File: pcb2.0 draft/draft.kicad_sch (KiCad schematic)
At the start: 24 parts, among them J1 Screw_Terminal_01x02, J2 Screw_Terminal_01x02, J3 Conn_01x04, J4 Conn_01x04, J5 Conn_01x04, U1 ESP32-DevKitC, U2 LM2576HVS-5, U3 LM2576HVS-3.3

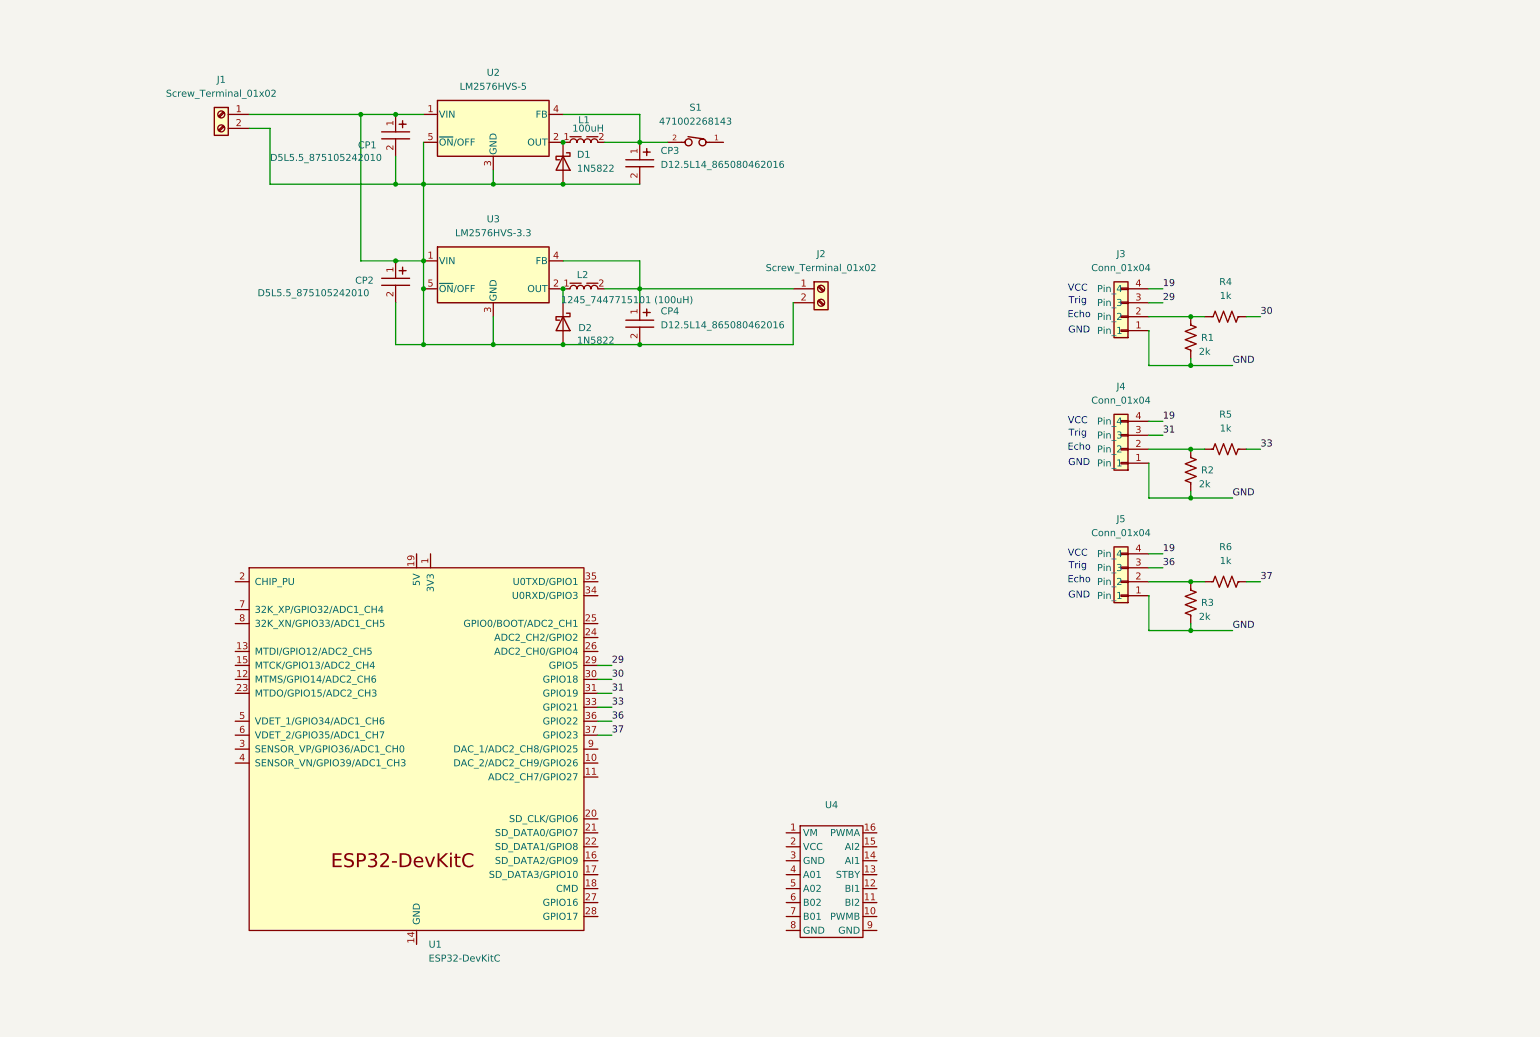
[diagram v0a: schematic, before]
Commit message: completed draft of pcbv2 - in "draft" folder
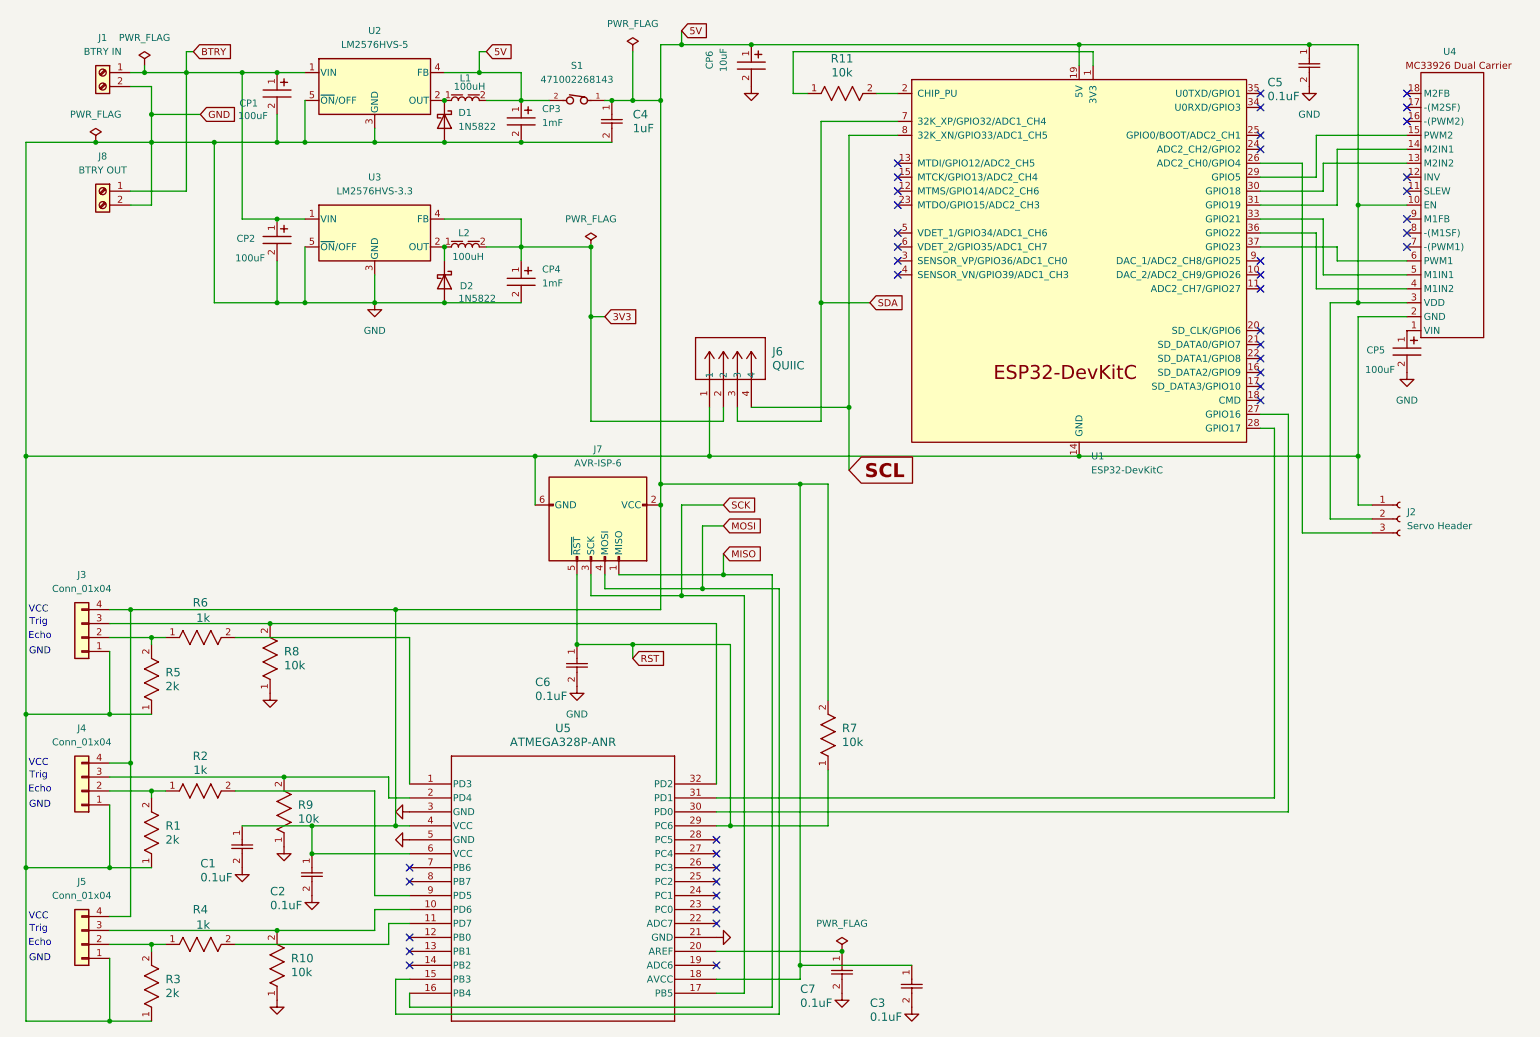
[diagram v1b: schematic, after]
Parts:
- removed J2: Screw_Terminal_01x02, terminal:CUI_TB002-500-02BE, symbol Connector:Screw_Terminal_01x02
- removed R1, R2, R3: 2k, Resistor_THT:R_Axial_DIN0207_L6.3mm_D2.5mm_P5.08mm_Vertical, symbol Device:R_US
- removed R4: 1k, Resistor_THT:R_Axial_DIN0207_L6.3mm_D2.5mm_P2.54mm_Vertical, symbol Device:R_US
- removed R5, R6: 1k, Resistor_THT:R_Axial_DIN0207_L6.3mm_D2.5mm_P5.08mm_Vertical, symbol Device:R_US
- removed U4: ~, custom:TB6612FNG_BoB, symbol custom:TB6612FNG_BoB
- added C1, C2, C3, C5, C6, C7: 0.1uF, G-188_MUR, symbol cap_murata_0603:GCM188R71C104KA37D
- added C4: 1uF, CAP_GRM21_MUR, symbol cap_murata_0805:GRM21BR71C105KA01L
- added CP5: 100uF, Capacitor_SMD_Wurth:CP_Wurth_WCAP-PSLP-D5L5.5, symbol WurthE:D5L5.5_875105242010
- added CP6: 10uF, Capacitor_SMD_Wurth:CP_Wurth_WCAP-PSLP-D5L5.8, symbol WurthE:D5L5.8_875105359001
- added J2: Servo Header, Connector_PinSocket_2.54mm:PinSocket_1x03_P2.54mm_Vertical, symbol Connector:Conn_01x03_Socket
- added J6: QUIIC, CONN_SM04B-SRSS-TB_JST, symbol quiic_jst:SM04B-SRSS-TB
- added J7: AVR-ISP-6, Connector_IDC:IDC-Header_2x03_P2.54mm_Vertical, symbol Connector:AVR-ISP-6
- added J8: BTRY OUT, terminal:CUI_TB002-500-02BE, symbol Connector:Screw_Terminal_01x02
- added R1, R3, R5: 2k, RES_CR0805_VEN, symbol R_SMD:CR0805-10W-2001FT
- added R10, R11, R7, R8, R9: 10k, RES_CR0805_VEN, symbol R_SMD:CR0805-10W-2001FT
- added R2, R4, R6: 1k, RES_CR0805_VEN, symbol R_SMD:CR0805-10W-2001FT
- added U4: ~, polulu_MC33926_dual:polulu_MC33926_dual, symbol polulu_MC33926_dual:MC33926_dual
- added U5: ATMEGA328P-ANR, 32A_ATM, symbol atmega328p-anr:ATMEGA328P-ANR
- CP1, CP2: value D5L5.5_875105242010 -> 100uF; footprint WurthE:CP_Wurth_WCAP-PSLP-D5L5.5 -> Capacitor_SMD_Wurth:CP_Wurth_WCAP-PSLP-D5L5.5
- CP3, CP4: value D12.5L14_865080462016 -> 1mF; footprint WurthE:CP_Wurth_WCAP-ASLI-D12.5L14 -> Capacitor_SMD_Wurth:CP_Wurth_WCAP-ASLI-D12.5L14
- J1: value Screw_Terminal_01x02 -> BTRY IN
- L1: footprint WE-PD:L_Wurth_WE-PD-1245 -> Inductor_SMD_Wurth:L_Wurth_WE-PD-1245
- L2: value 1245_7447715101 (100uH) -> 100uH; footprint WE-PD:L_Wurth_WE-PD-1245 -> Inductor_SMD_Wurth:L_Wurth_WE-PD-1245
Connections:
- net 19 is gone; now on net 5V: J3.4 (Pin_4), J4.4 (Pin_4), J5.4 (Pin_4)
- net GND: now also CP1.2, CP2.2, CP3.2, CP4.2, D1.2 (A), D2.2 (A), J1.2 (Pin_2), U1.14 (GND), U1.32 (GND), U1.38 (GND), U2.3 (GND), U2.5 (~{ON}/OFF), U3.3 (GND), U3.5 (~{ON}/OFF), C1.2, C2.2, C3.2, C4.2, C5.2, C6.2, C7.2, CP5.2, CP6.2, J2.1 (Pin_1), J6.1, J7.6 (GND), J8.2 (Pin_2), R1.1, R10.1, R3.1, R5.1, R8.1, R9.1, U4.2 (GND), U5.21 (GND), U5.3 (GND), U5.5 (GND)
- net at J5.2 (Pin_2): now also R3.2, R4.1
- net 5V: now reaches CP3.1, L1.2, S1.2, U2.4 (FB)
- net 5V: now also S1.1, U1.19 (5V), C1.1, C2.1, C3.1, C4.1, C5.1, CP6.1, J2.2 (Pin_2), J7.2 (VCC), R7.2, U4.10 (EN), U4.3 (VDD), U5.18 (AVCC), U5.4 (VCC), U5.6 (VCC)
- net 3V3: now reaches CP4.1, L2.2, U3.4 (FB)
- net 3V3: now also J6.2
- net at J3.2 (Pin_2): now also R5.2, R6.1
- net at J4.2 (Pin_2): now also R1.2, R2.1
- net at U1.1 (3V3): now also R11.1
- net at U1.2 (CHIP_PU): now also R11.2
- net at U1.26 (ADC2_CH0/GPIO4): now also J2.3 (Pin_3)
- net at U1.27 (GPIO16): now also U5.30 (PD0)
- net at U1.28 (GPIO17): now also U5.31 (PD1)
- net SDA: now reaches U1.7 (32K_XP/GPIO32/ADC1_CH4)
- net SDA: now also J6.3
- net SCL: now reaches U1.8 (32K_XN/GPIO33/ADC1_CH5)
- net SCL: now also J6.4
- net 29: no longer names the net of J3.3 (Pin_3)
- net 29: now also R8.2, U5.32 (PD2); no longer U1.29 (GPIO5)
- net 30: no longer names the net of U1.30 (GPIO18)
- net 30: now also U4.13 (M2IN2)
- net 31: no longer names the net of J4.3 (Pin_3)
- net 31: now also R9.2, U5.2 (PD4); no longer U1.31 (GPIO19)
- net 33: no longer names the net of U1.33 (GPIO21)
- net 33: now also U4.5 (M1IN1)
- net 36: no longer names the net of J5.3 (Pin_3)
- net 36: now also R10.2, U5.10 (PD6); no longer U1.36 (GPIO22)
- net 37: no longer names the net of U1.37 (GPIO23)
- net 37: now also U4.6 (PWM1)
- new net: R6.2, U5.1 (PD3)
- new net: R4.2, U5.11 (PD7)
- new net: C7.1, U5.20 (AREF)
- new net: R2.2, U5.9 (PD5)
- new net: U1.29 (GPIO5), U4.15 (PWM2)
- new net: U1.31 (GPIO19), U4.14 (M2IN1)
- new net: U1.36 (GPIO22), U4.4 (M1IN2)
- new net: CP5.1, U4.1 (VIN)
- new net BTRY: CP1.1, CP2.1, J1.1 (Pin_1), J8.1 (Pin_1), U2.1 (VIN), U3.1 (VIN)
- new net MISO: J7.1 (MISO), U5.16 (PB4)
- new net MOSI: J7.4 (MOSI), U5.15 (PB3)
- new net RST: C6.1, J7.5 (~{RST}), R7.1, U5.29 (PC6)
- new net SCK: J7.3 (SCK), U5.17 (PB5)
- no-connect marks 0 -> 42
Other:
- title: (none) -> PCB Version 2.0
- moved on the sheet: CP1, CP2, CP3, CP4, D1, D2, J1, L1, L2, S1, U1, U2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

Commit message: some more schematic updates
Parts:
- removed S1: 471002268143, WE-RSTV:switch_471002268143_actual, symbol WE-RSTV:471002268143
- added C8: 1uF, CAP_GRM21_MUR, symbol cap_murata_0805:GRM21BR71C105KA01L
- added LED1, LED2, LED3, LED4: EAST3215BA3, LEDC3215X110N, symbol Everlight_LED_1206:EAST3215BA3
- added R12: 1.2k, ERJU08J122V:RES_ERJU08J122V, symbol R_panasonic_1206_1p2k:ERJU08J122V
- added R13: 620, RC1206N_PAN, symbol R_panasonic_1206_620:ERJ-P08J621V
- added R14, R15: 270, ERJU08J271V:RES_ERJU08J271V, symbol R_panasonic_1206_270:ERJU08J271V
- added R16, R17: 10k, RES_CR0805_VEN, symbol R_SMD:CR0805-10W-2001FT
- added S2, S3: EG2201B, EG2201B:SW_EG2201B, symbol SW_eswitch_dpdt_eg2201:EG2201B
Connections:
- net 3V3: now also C1.1, C2.1, C3.1, J3.4 (Pin_4), J4.4 (Pin_4), J5.4 (Pin_4), J7.2 (VCC), R7.2, U5.18 (AVCC), U5.4 (VCC), U5.6 (VCC), C8.1, LED3.2 (A), S3.4, S3.5
- net 5V: now also LED2.2 (A), S3.1, S3.2; no longer C1.1, C2.1, C3.1, J3.4 (Pin_4), J4.4 (Pin_4), J5.4 (Pin_4), J7.2 (VCC), R7.2, U5.18 (AVCC), U5.4 (VCC), U5.6 (VCC)
- net BTRY: now also LED1.2 (A)
- net GND: now also C8.2, R12.1, R13.2, R14.2, R15.2, R16.1, R17.1
- net at U5.27 (PC4): now also LED4.2 (A)
- net at U5.30 (PD0): now also S2.5; no longer U1.27 (GPIO16)
- net at U5.31 (PD1): now also S2.2; no longer U1.28 (GPIO17)
- new net: R17.2, S2.6
- new net: LED4.1 (K), R15.1
- new net: S2.1, U1.28 (GPIO17)
- new net: R16.2, S2.3
- new net: S2.4, U1.27 (GPIO16)
- new net: LED1.1 (K), R12.2
- new net: LED2.1 (K), R13.1
- new net: LED3.1 (K), R14.1
- no-connect marks 42 -> 41
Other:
- note added: "ADD REVERSE POLARITY PROTECTION"
- moved on the sheet: C4, CP6

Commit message: completed pcb layout
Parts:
- removed J1: BTRY IN, terminal:CUI_TB002-500-02BE, symbol Connector:Screw_Terminal_01x02
- removed J8: BTRY OUT, terminal:CUI_TB002-500-02BE, symbol Connector:Screw_Terminal_01x02
- added J1: BTRY IN, jst_xh:JST_B2B-XH-A, symbol JST_XH-A:B2B-XH-A
- added J8: BTRY OUT, jst_xh:JST_B2B-XH-A, symbol JST_XH-A:B2B-XH-A
- C1, C2, C3, C5, C6, C7: footprint G-188_MUR -> cap_murata_0603:G-188_MUR-L
- C4, C8: footprint CAP_GRM21_MUR -> cap_murata_0805:CAP_GRM21_MUR-L
- CP1, CP2, CP5: footprint Capacitor_SMD_Wurth:CP_Wurth_WCAP-PSLP-D5L5.5 -> WurthE:CP_Wurth_WCAP-PSLP-D5L5.5
- CP3, CP4: footprint Capacitor_SMD_Wurth:CP_Wurth_WCAP-ASLI-D12.5L14 -> WurthE:CP_Wurth_WCAP-ASLI-D12.5L14
- CP6: footprint Capacitor_SMD_Wurth:CP_Wurth_WCAP-PSLP-D5L5.8 -> WurthE:CP_Wurth_WCAP-PSLP-D5L5.8
- J6: footprint CONN_SM04B-SRSS-TB_JST -> quiic_jst:CONN_SM04B-SRSS-TB_JST
- L1, L2: footprint Inductor_SMD_Wurth:L_Wurth_WE-PD-1245 -> WE-PD:L_Wurth_WE-PD-1245
- LED1, LED2, LED3, LED4: footprint LEDC3215X110N -> led_smd_1206:LEDC3215X110N
- R1, R10, R11, R16, R17, R2, R3, R4, R5, R6, R7, R8, R9: footprint RES_CR0805_VEN -> R_SMD:RES_CR0805_VEN-L
- R12: footprint ERJU08J122V:RES_ERJU08J122V -> r_erj_1p2k:RES_ERJU08J122V
- R13: footprint RC1206N_PAN -> R_ERJ_620_1206:RC1206N_PAN-L
- R14, R15: footprint ERJU08J271V:RES_ERJU08J271V -> r_erj_270:RES_ERJU08J271V
- S2, S3: footprint EG2201B:SW_EG2201B -> switch_eg2201_dpdt:SW_EG2201B
- U5: footprint 32A_ATM -> atmega328p-anr:32A_ATM-L
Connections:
- net 3V3: no longer CP4.1, L2.2, S3.5, U3.4 (FB)
- net 5V: no longer CP3.1, L1.2, S3.2, U2.4 (FB)
- net BTRY: now also J1.2, J8.2
- net GND: now also J1.1, J8.1
- new net 3V30: CP4.1, L2.2, S3.5, U3.4 (FB)
- new net 5V0: CP3.1, L1.2, S3.2, U2.4 (FB)
- no-connect marks 41 -> 43

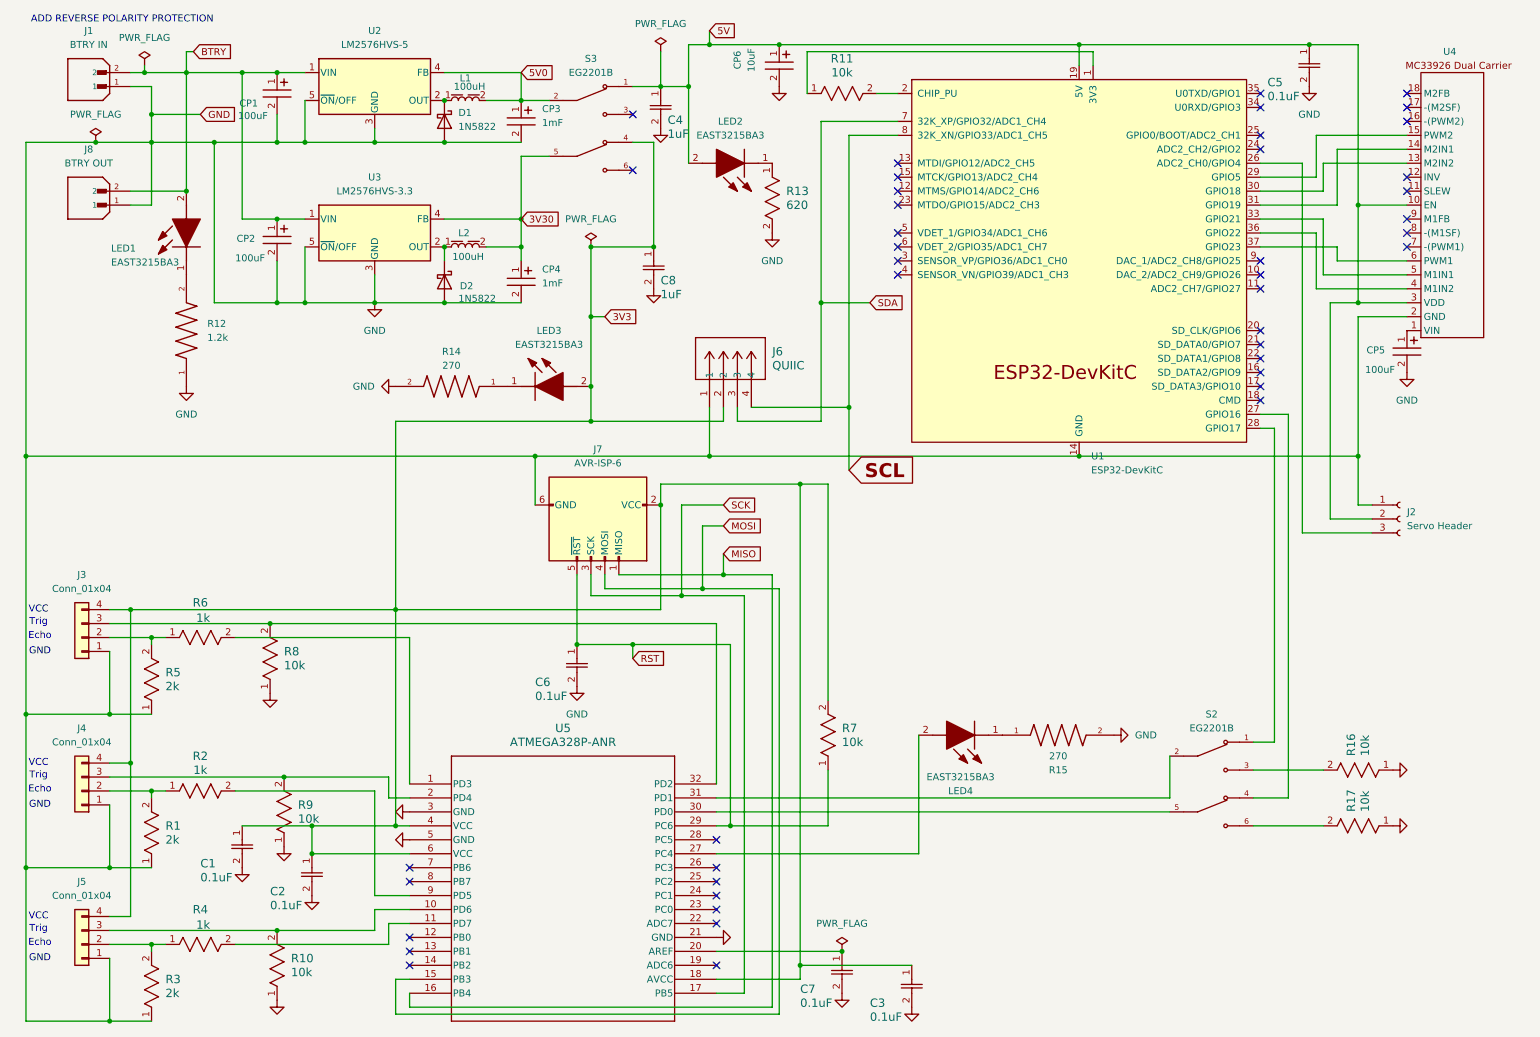
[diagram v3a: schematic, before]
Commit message: broke out code into header files
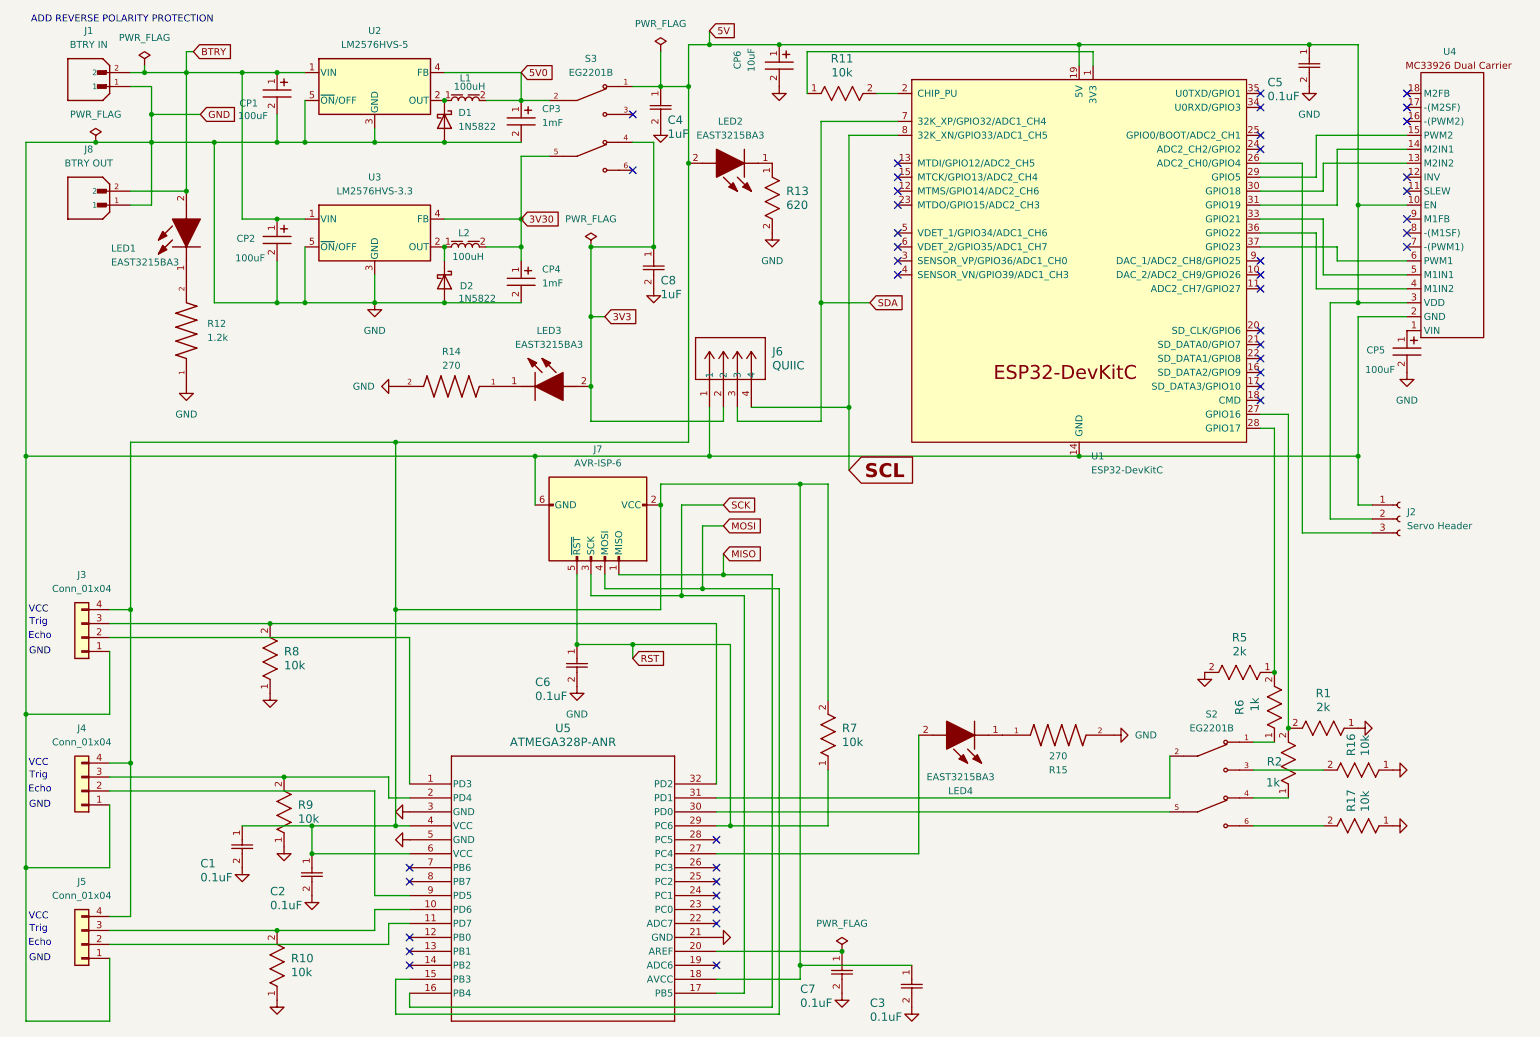
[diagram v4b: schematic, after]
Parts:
- removed R3: 2k, R_SMD:RES_CR0805_VEN-L, symbol R_SMD:CR0805-10W-2001FT
- removed R4: 1k, R_SMD:RES_CR0805_VEN-L, symbol R_SMD:CR0805-10W-2001FT
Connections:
- net 3V3: no longer C1.1, C2.1, C3.1, J3.4 (Pin_4), J4.4 (Pin_4), J5.4 (Pin_4), J7.2 (VCC), R7.2, U5.18 (AVCC), U5.4 (VCC), U5.6 (VCC)
- net 5V: now also C1.1, C2.1, C3.1, J3.4 (Pin_4), J4.4 (Pin_4), J5.4 (Pin_4), J7.2 (VCC), R7.2, U5.18 (AVCC), U5.4 (VCC), U5.6 (VCC)
- net GND: now also R5.2; no longer R5.1
- net at U5.1 (PD3): now also J3.2 (Pin_2); no longer R6.2
- net at U5.11 (PD7): now also J5.2 (Pin_2)
- net at U5.9 (PD5): now also J4.2 (Pin_2); no longer R2.2
- net at S2.1: now also R6.1; no longer U1.28 (GPIO17)
- net at S2.4: now also R2.1; no longer U1.27 (GPIO16)
- new net: R5.1, R6.2, U1.28 (GPIO17)
- new net: R1.2, R2.2, U1.27 (GPIO16)
